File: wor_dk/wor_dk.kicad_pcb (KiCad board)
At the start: 4 copper layers, 217 x 110.1 mm, 139 parts, among them J101 Conn_01x02, J102 Conn_02x03_Odd_Even, J103 Conn_02x03_Odd_Even, J104 Conn_01x02, J201 SWD, J301 SMA, J302 Conn_02x04_Odd_Even, J303 Conn_02x06_Odd_Even, J401 USB_C_Receptacle_USB2.0_16P, J501 SWD, J502 USB_C_Receptacle_USB2.0_16P, J503 SWD, Q501 BSS84, SW201 SW_Push, SW501 SW_Push, U201 nRF52840, U202 TMUX1112PWR, U203 TMUX1112PWR, U301 Si4467, U401 FT232RL, U501 TLV1117-33, U502 LPC11U35FHI33_501, Y201 32.768kHz, Y202 32MHz, Y301 26MHz, Y501 12MHz

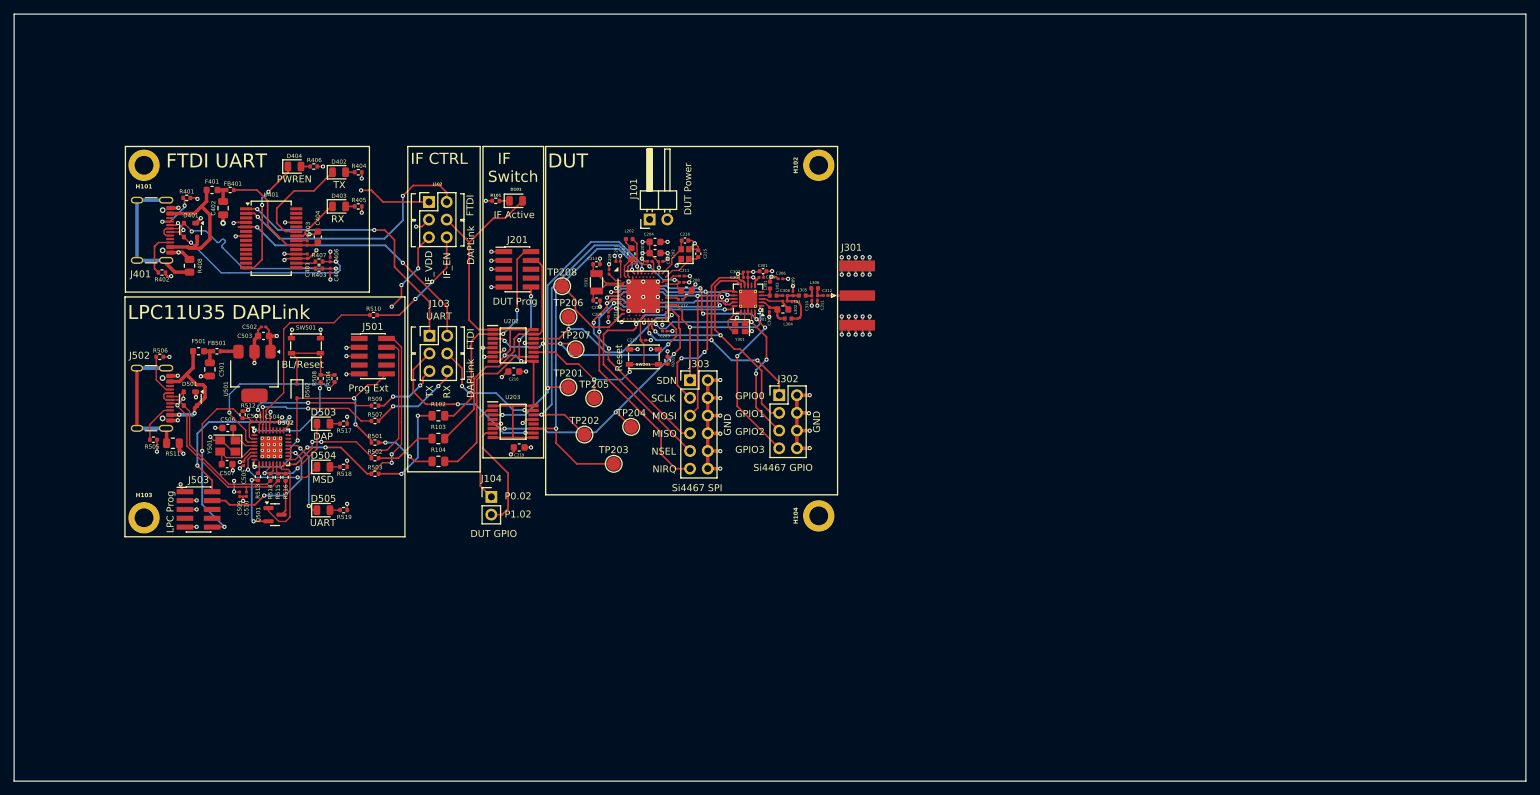
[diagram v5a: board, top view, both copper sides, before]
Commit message: wor_dk: PCB: adjust board outline
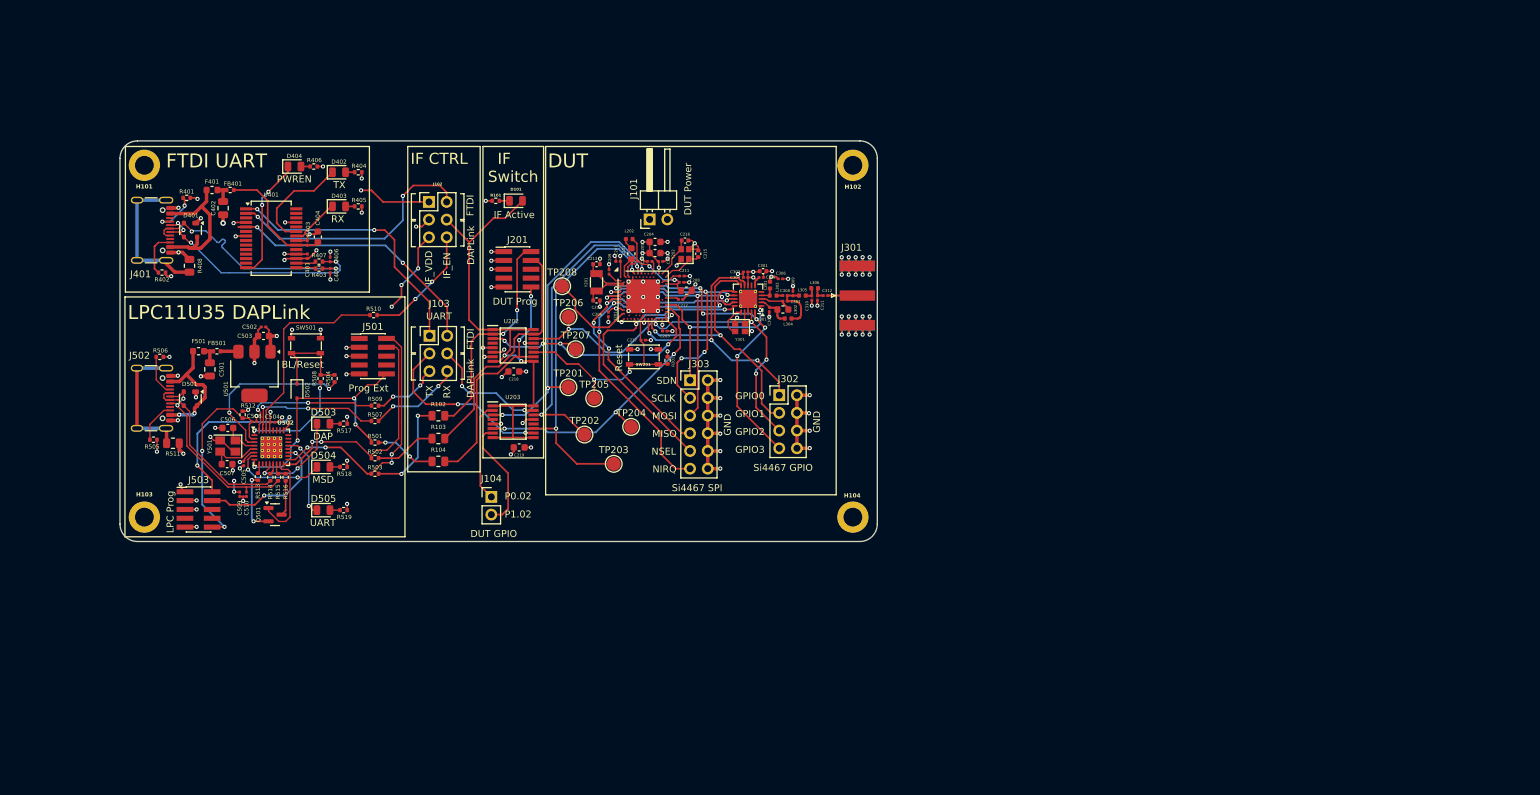
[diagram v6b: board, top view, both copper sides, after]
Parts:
- moved H104 4.90 mm to (160.6, 108.3)
- moved H102 4.90 mm to (160.6, 57.8)
- moved H103 0.11 mm to (58.9, 108.3)
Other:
- board size 217 x 110.1 mm -> 108.7 x 57.5 mm
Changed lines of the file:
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@@
 	(footprint "MountingHole:MountingHole_2.7mm_M2.5_ISO7380_Pad"
 		(layer "F.Cu")
-		(at 58.85 108.4)
+		(at 58.9 108.3)
 		(descr "Mounting Hole 2.7mm, M2.5, ISO7380")
 		(tags "mounting hole 2.7mm m2.5 iso7380")
@@
 	(footprint "MountingHole:MountingHole_2.7mm_M2.5_ISO7380_Pad"
 		(layer "F.Cu")
-		(at 155.7 108.125)
+		(at 160.6 108.3)
 		(descr "Mounting Hole 2.7mm, M2.5, ISO7380")
 		(tags "mounting hole 2.7mm m2.5 iso7380")
 		(property "Reference" "H104"
-			(at -3.3 -0.025 90)
+			(at -0.1 -3.1 180)
 			(layer "F.SilkS")
 			(effects
@@
 	(footprint "MountingHole:MountingHole_2.7mm_M2.5_ISO7380_Pad"
 		(layer "F.Cu")
-		(at 58.85 57.8)
+		(at 58.9 57.8)
 		(descr "Mounting Hole 2.7mm, M2.5, ISO7380")
 		(tags "mounting hole 2.7mm m2.5 iso7380")
@@
 	(footprint "MountingHole:MountingHole_2.7mm_M2.5_ISO7380_Pad"
 		(layer "F.Cu")
-		(at 155.7 57.8)
+		(at 160.6 57.8)
 		(descr "Mounting Hole 2.7mm, M2.5, ISO7380")
 		(tags "mounting hole 2.7mm m2.5 iso7380")
 		(property "Reference" "H102"
-			(at -3.3 0 90)
+			(at 0 3.1 180)
 			(layer "F.SilkS")
 			(effects
@@
 	(gr_rect
 		(start 116.5 55.1)
-		(end 158.4 105.1)
+		(end 158.2 105.1)
 		(stroke
 			(width 0.1)
@@
 		(layer "F.SilkS")
 	)
-	(gr_rect
-		(start 40.2 36.1)
-		(end 257.2 146.2)
+	(gr_arc
+		(start 55.4 56.8)
+		(mid 56.132233 55.032233)
+		(end 57.9 54.3)
+		(stroke
+			(width 0.05)
+			(type default)
+		)
+		(layer "Edge.Cuts")
+	)
+	(gr_arc
+		(start 164.1 109.3)
+		(mid 163.367767 111.067767)
+		(end 161.6 111.8)
+		(stroke
+			(width 0.05)
+			(type default)
+		)
+		(layer "Edge.Cuts")
+	)
+	(gr_arc
+		(start 161.6 54.3)
+		(mid 163.367767 55.032233)
+		(end 164.1 56.8)
+		(stroke
+			(width 0.05)
+			(type default)
+		)
+		(layer "Edge.Cuts")
+	)
+	(gr_line
+		(start 55.4 109.3)
+		(end 55.4 56.8)
+		(stroke
+			(width 0.05)
+			(type default)
+		)
+		(layer "Edge.Cuts")
+	)
+	(gr_line
+		(start 161.6 111.8)
+		(end 57.9 111.8)
+		(stroke
+			(width 0.05)
+			(type default)
+		)
+		(layer "Edge.Cuts")
+	)
+	(gr_line
+		(start 57.9 54.3)
+		(end 161.6 54.3)
+		(stroke
+			(width 0.05)
+			(type default)
+		)
+		(layer "Edge.Cuts")
+	)
+	(gr_line
+		(start 164.1 56.8)
+		(end 164.1 109.3)
+		(stroke
+			(width 0.05)
+			(type default)
+		)
+		(layer "Edge.Cuts")
+	)
+	(gr_arc
+		(start 57.9 111.8)
+		(mid 56.132233 111.067767)
+		(end 55.4 109.3)
 		(stroke
 			(width 0.05)
 			(type default)
 		)
-		(fill none)
 		(layer "Edge.Cuts")
 	)

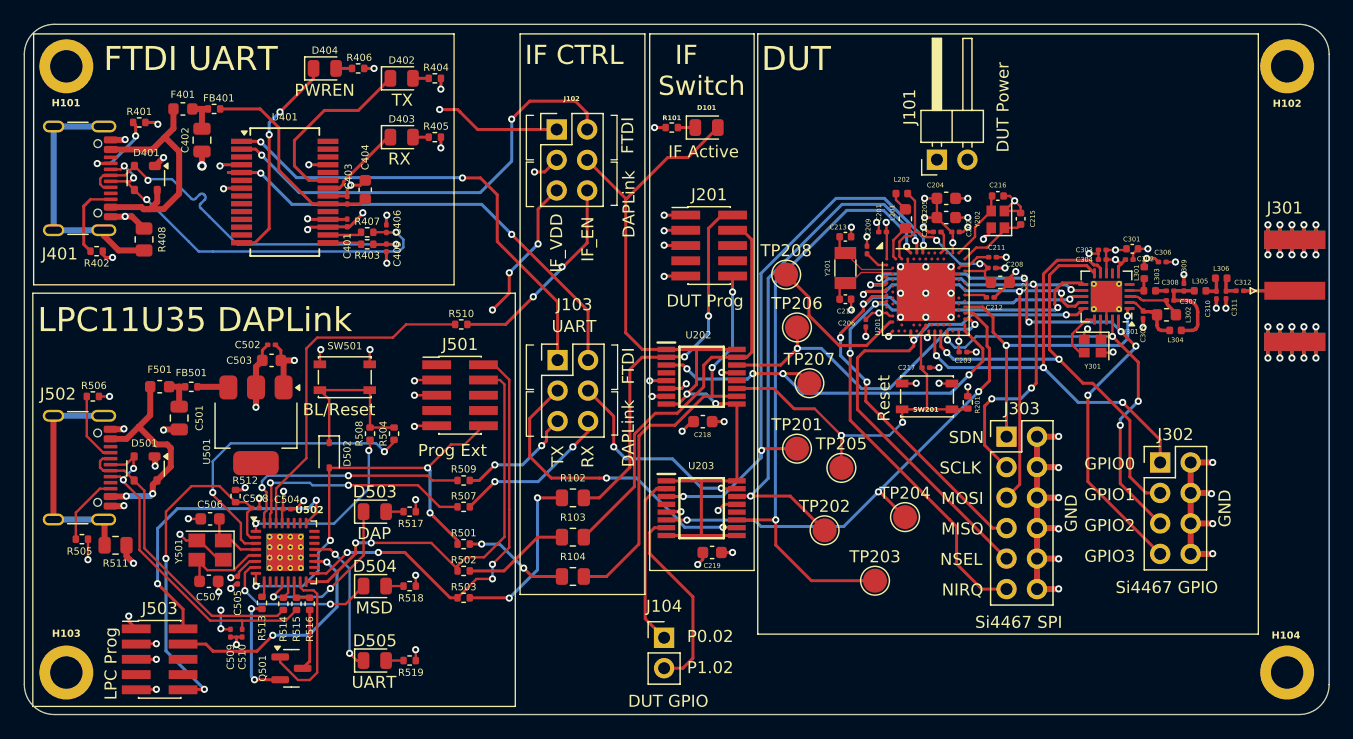
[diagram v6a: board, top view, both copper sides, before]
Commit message: wor_dk: PCB: add guard rail for transceiver parts
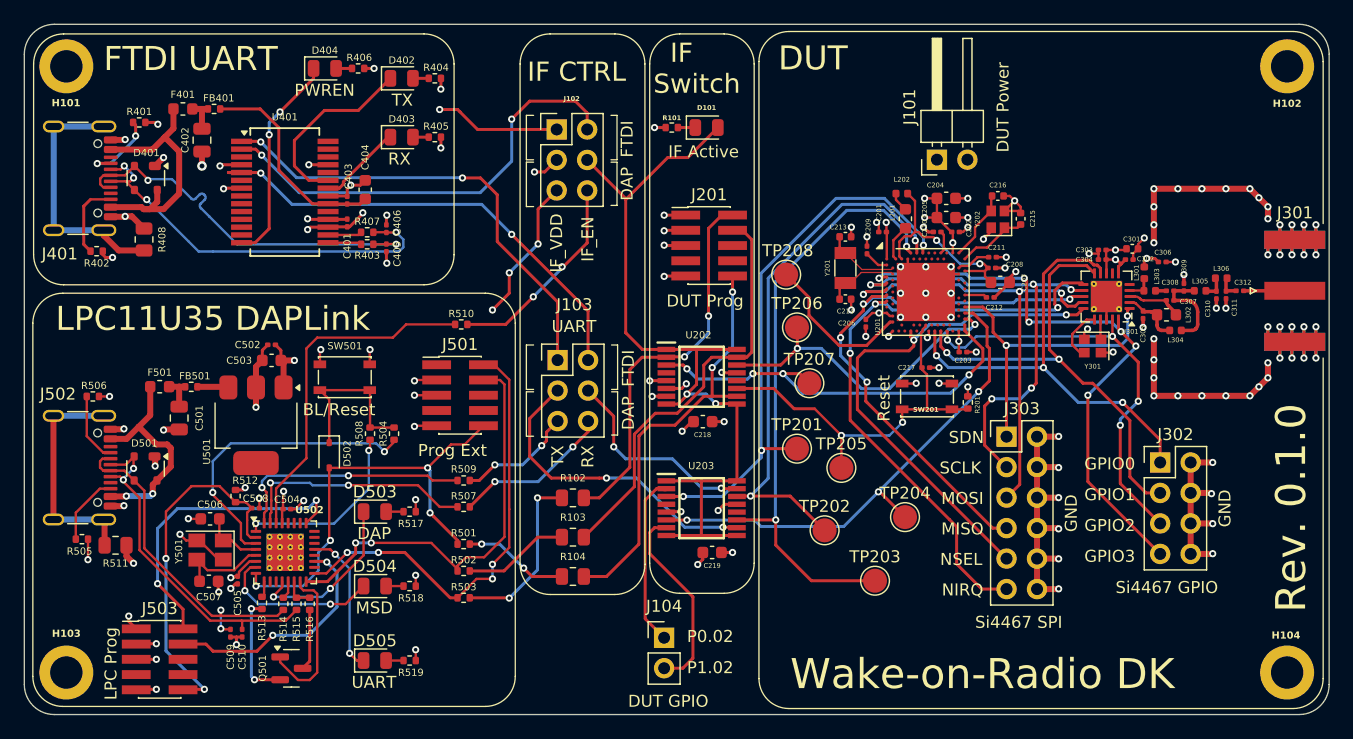
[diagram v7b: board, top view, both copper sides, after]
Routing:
- net GND: track 214.3 -> 245.7 mm, vias 110 -> 130
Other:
- board text added: "Rev. 0.1.0"
- board text added: "Wake-on-Radio DK"
- board text removed: "DAPLink"
